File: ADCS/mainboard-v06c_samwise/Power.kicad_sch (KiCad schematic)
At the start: 53 parts, among them J14 Conn_01x08_Horizontal, J19 35362-0650, U17 BQ25883RGER, U21 TPS7A4501DCQT, U4 ADM1176-1ARMZ-R7, U5 TPS54226PWPR, U6 LT3652HVIMSE#PBF

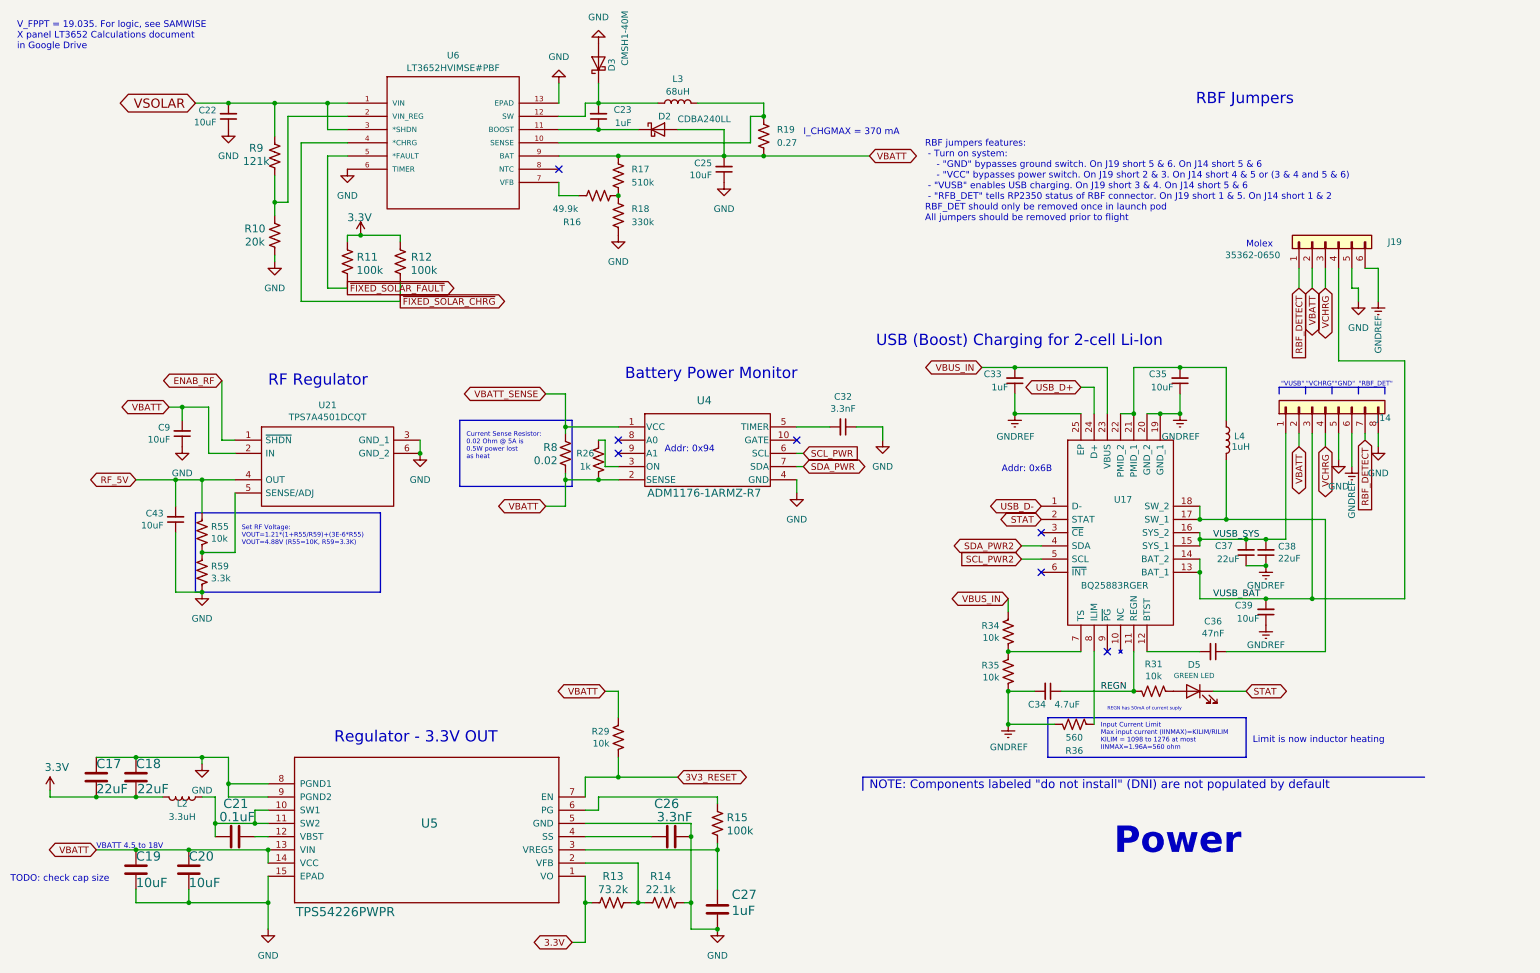
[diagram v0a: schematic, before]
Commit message: mainboard updates removed a bunch of stuff
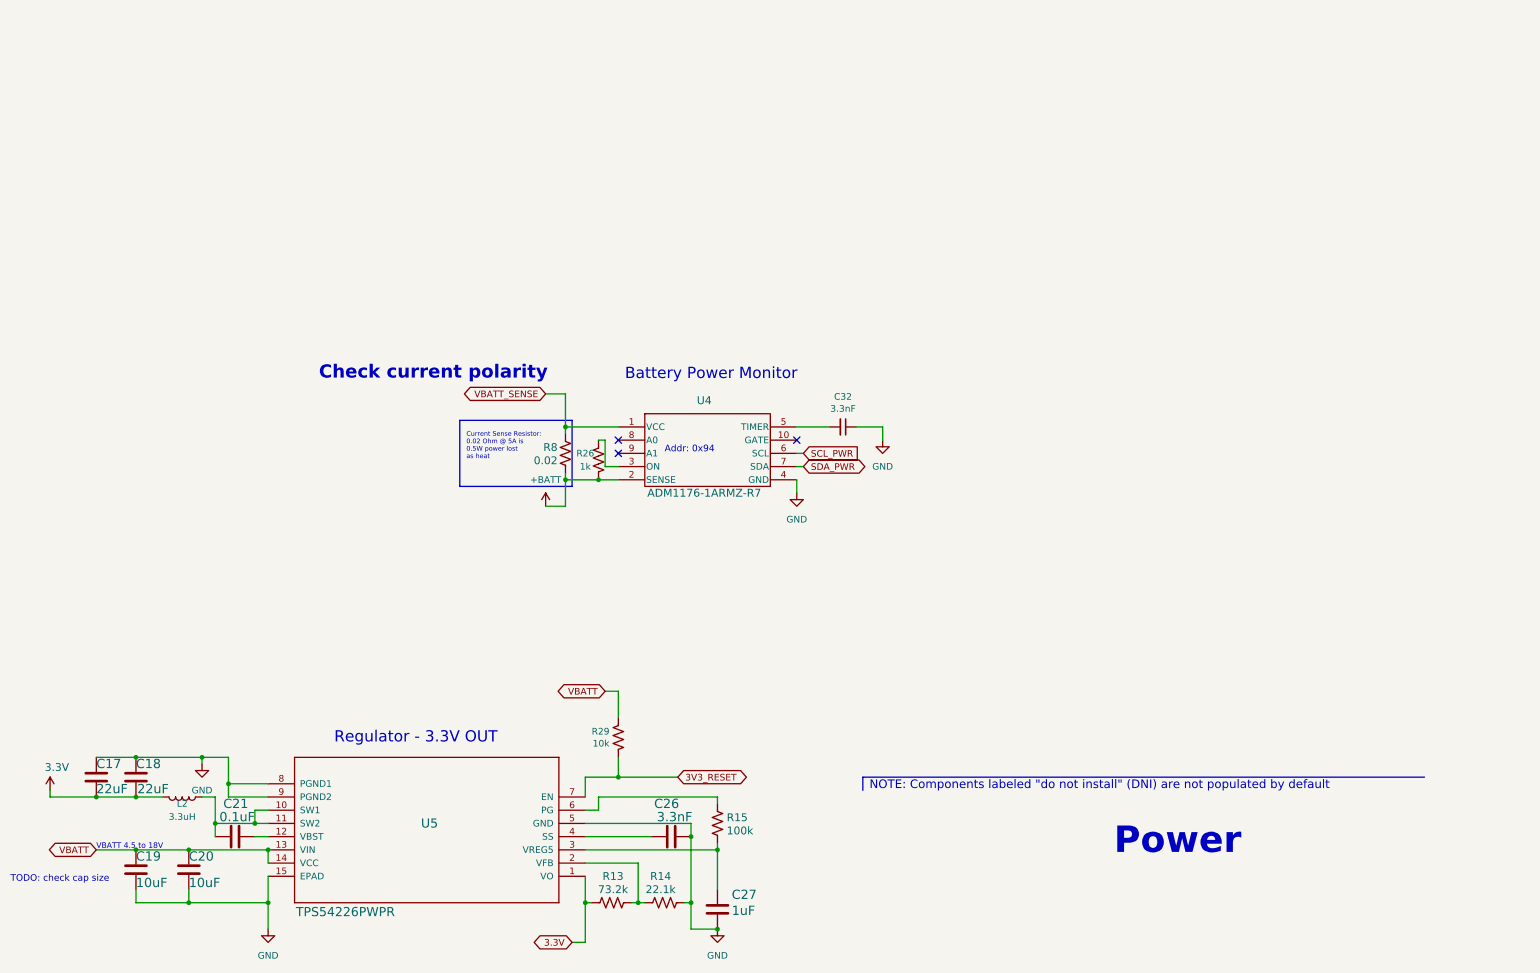
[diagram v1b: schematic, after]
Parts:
- removed C22: 10uF, Capacitor_SMD:C_1210_3225Metric, symbol Device:C_Small
- removed C23, C33: 1uF, Capacitor_SMD:C_0603_1608Metric, symbol Device:C_Small
- removed C25, C35, C39, C43, C9: 10uF, Capacitor_SMD:C_0603_1608Metric, symbol Device:C_Small
- removed C34: 4.7uF, Capacitor_SMD:C_0603_1608Metric, symbol Device:C_Small
- removed C36: 47nF, Capacitor_SMD:C_0603_1608Metric, symbol Device:C_Small
- removed C37, C38: 22uF, Capacitor_SMD:C_0603_1608Metric, symbol Device:C_Small
- removed D2: CDBA240LL, ssi_diode:DO-214AC, symbol Device:D_Schottky
- removed D3: CMSH1-40M, ssi_diode:DIOM5226X262N, symbol Device:D_Schottky
- removed D5: GREEN LED, LED_SMD:LED_0603_1608Metric, symbol Device:LED
- removed J14: Conn_01x08_Horizontal, Connector_PinHeader_2.54mm:PinHeader_1x08_P2.54mm_Horizontal, symbol Connector_Generic:Conn_01x08
- removed J19: 35362-0650, ssi_connector:Molex_35362-0650, symbol Connector_Generic:Conn_01x06
- removed L3: 68uH, ssi_inductor:SDE06004A-680K, symbol Device:L
- removed L4: 1uH, ssi_inductor:L_2510, symbol Device:L
- removed R10: 20k, Resistor_SMD:R_0603_1608Metric, symbol Device:R_US
- removed R11, R12: 100k, Resistor_SMD:R_0603_1608Metric, symbol Device:R_US
- removed R16: 49.9k, Resistor_SMD:R_0603_1608Metric, symbol Device:R_US
- removed R17: 510k, Resistor_SMD:R_0603_1608Metric, symbol Device:R_US
- removed R18: 330k, Resistor_SMD:R_0603_1608Metric, symbol Device:R_US
- removed R19: 0.27, Resistor_SMD:R_2512_6332Metric, symbol Device:R_US
- removed R31, R34, R35, R55: 10k, Resistor_SMD:R_0603_1608Metric, symbol Device:R_US
- removed R36: 560, Resistor_SMD:R_0603_1608Metric, symbol Device:R_US
- removed R59: 3.3k, Resistor_SMD:R_0603_1608Metric, symbol Device:R_US
- removed R9: 121k, Resistor_SMD:R_0603_1608Metric, symbol Device:R_US
- removed U17: BQ25883RGER, ssi_IC:QFN50P400X400X100-25N-D, symbol ssi_IC:BQ25883RGER
- removed U21: TPS7A4501DCQT, ssi_IC:TPS7A4501DCQT, symbol ssi_IC:TPS7A4501DCQT
- removed U6: LT3652HVIMSE#PBF, ssi_IC:MSOP-12_MSE, symbol ssi_IC:LT3652HVIMSE#PBF
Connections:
- net VBATT: no longer R26.1, R8.1, U4.2 (SENSE)
- new net +BATT: R26.1, R8.1, U4.2 (SENSE)
- no-connect marks 7 -> 3
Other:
- note added: "Check current polarity"
- note removed: ""GND""
- note removed: ""RBF_DET""
- note removed: ""VCHRG""
- note removed: ""VUSB""
- note removed: "Addr: 0x6B"
- note removed: "I_CHGMAX = 370 mA"
- note removed: "Input Current Limit Max input current (IINMAX)=KILIM/RILIM KILIM = 1098 to 1276 at most IINMAX=1.96A=560 ohm"
- note removed: "Limit is now inductor heating"
- note removed: "Molex"
- note removed: "RBF Jumpers"
- note removed: "RBF jumpers features: - Turn on system: - "GND" bypasses ground switch. On J19 short 5 & 6. On J14 short 5 & 6 - "VCC" bypasses power switch. On J19 short 2 & 3. On J14 short 4 & 5 or (3 & 4 and 5 & 6) - "VUSB" enables USB charging. On J19 short 3 & 4. On J14 short 5 & 6 - "RFB_DET" tells RP2350 status of RBF connector. On J19 short 1 & 5. On J14 short 1 & 2 RBF_DET should only be removed once in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"
- note removed: "REGN has 50mA of current suply"
- note removed: "RF Regulator"
- note removed: "Set RF Voltage: VOUT=1.21*(1+R55/R59)+(3E-6*R55) VOUT=4.88V (R55=10K, R59=3.3K)"
- note removed: "USB (Boost) Charging for 2-cell Li-Ion"
- note removed: "V_FPPT = 19.035. For logic, see SAMWISE X panel LT3652 Calculations document in Google Drive"
